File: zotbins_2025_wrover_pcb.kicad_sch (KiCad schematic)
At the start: 18 parts, among them J1 ov2640, J2 hcsr04, J3 hx711, J4 infrared, U1 ESP32-WROVER-E/IE-DEVKIT-C, U2 MCP23017_SP, U3 XC6206P122MR-G, U4 XC6206P282PR-G

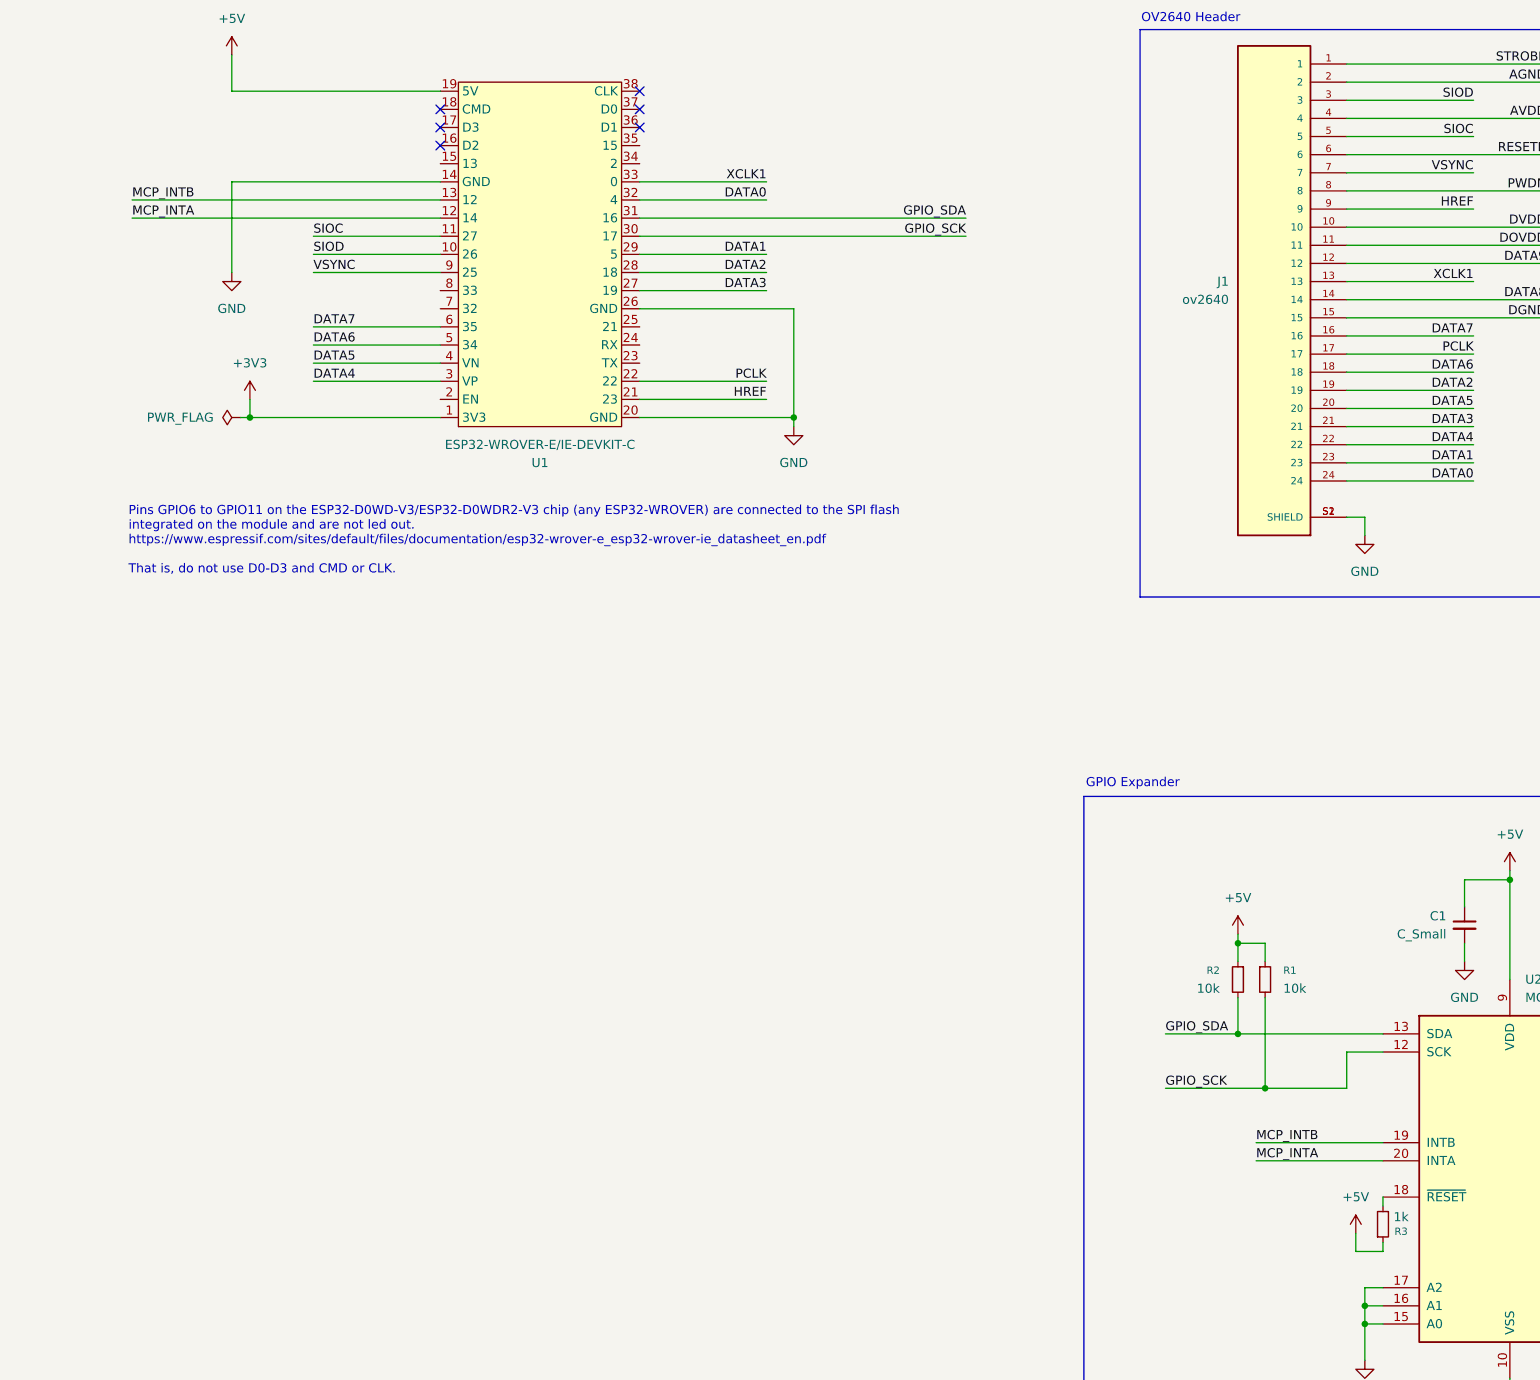
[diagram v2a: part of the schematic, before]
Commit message: pins reconfigured
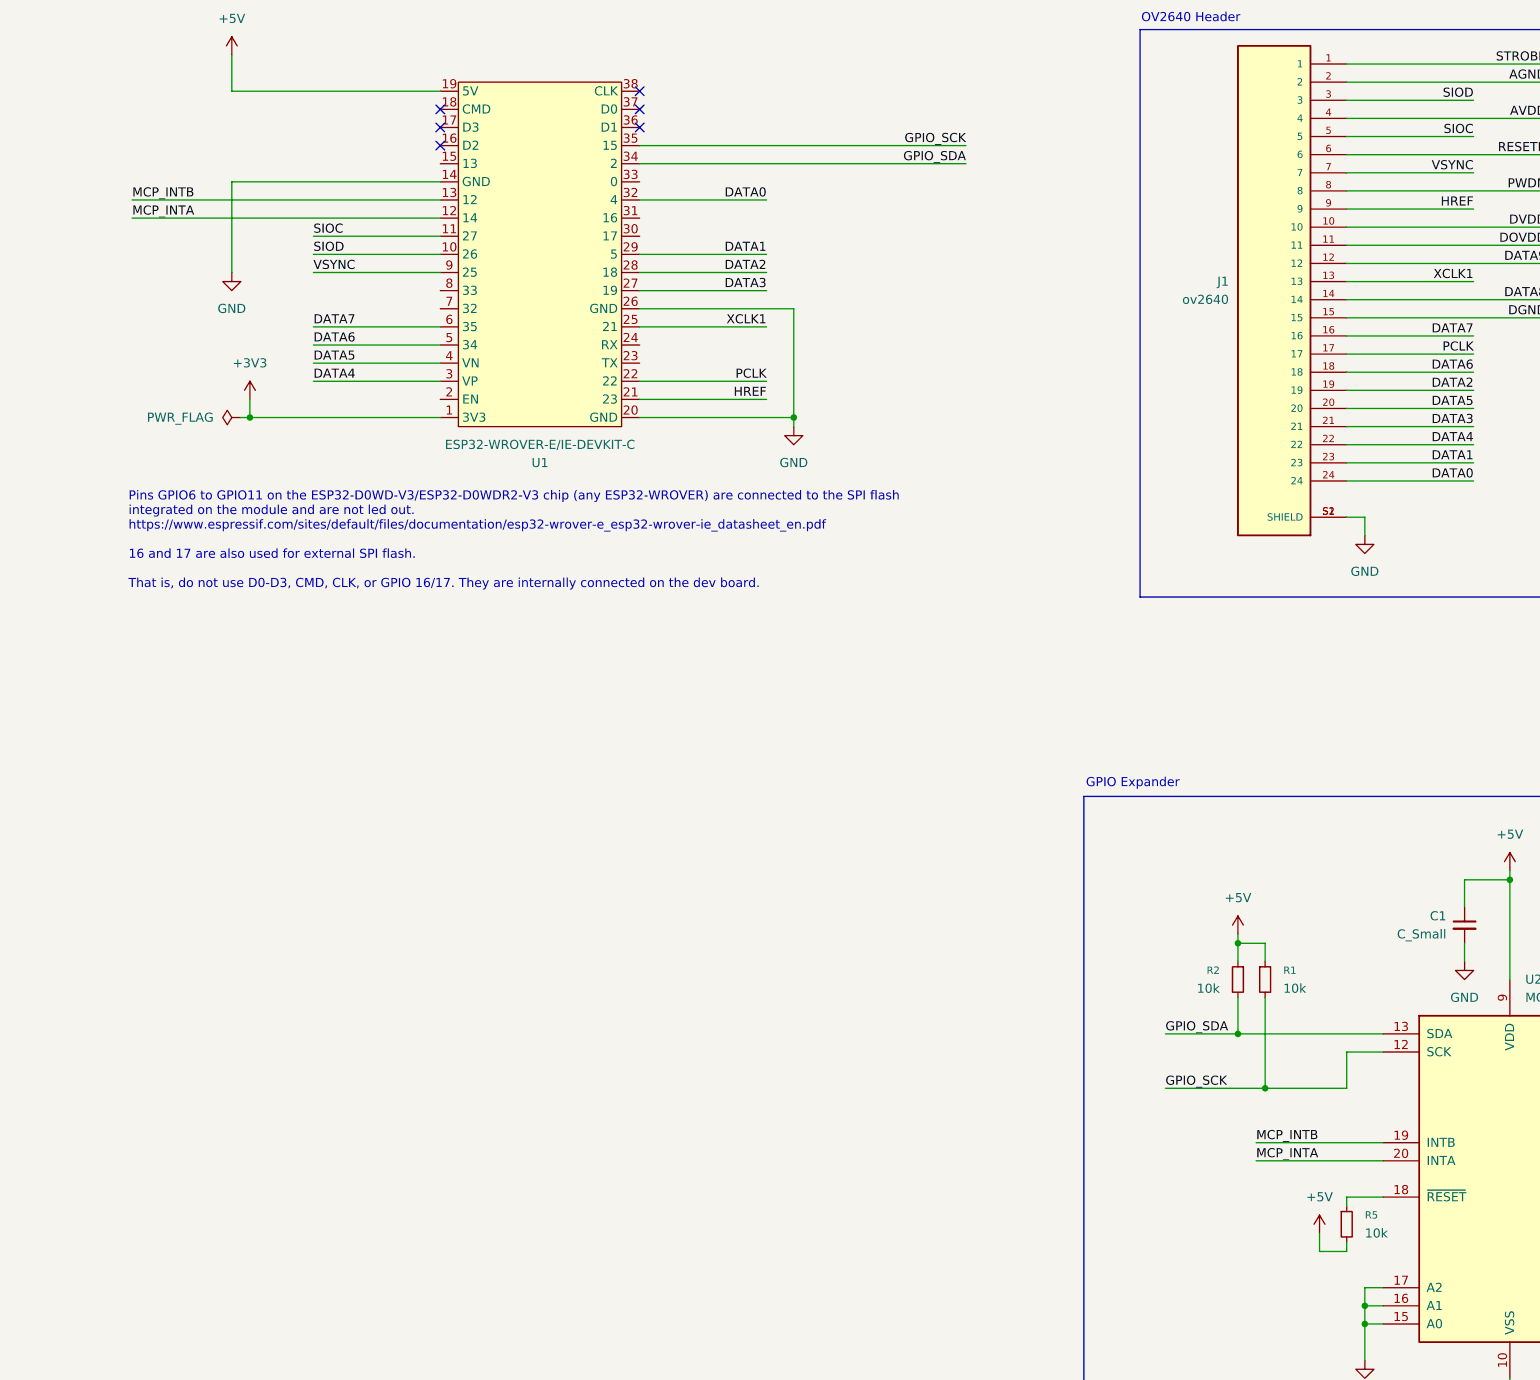
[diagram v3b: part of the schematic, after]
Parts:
- removed R3: 1k, symbol Device:R_Small
- added R5: 10k, symbol Device:R_Small
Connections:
- net +5V: now also R5.2
- net GPIO_SCK: now also U1.35 (15); no longer U1.30 (17)
- net GPIO_SDA: now also U1.34 (2); no longer U1.31 (16)
- net XCLK1: now also U1.25 (21); no longer U1.33 (0)
- net at U2.18 (~{RESET}): now also R5.1
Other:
- note added: "Pins GPIO6 to GPIO11 on the ESP32-D0WD-V3/ESP32-D0WDR2-V3 chip (any ESP32-WROVER) are connected to the SPI flash integrated on the module and are not led out. https://www.espressif.com/sites/default/files/documentation/esp32-wrover-e_esp32-wrover-ie_datasheet_en.pdf 16 and 17 are also used for external SPI flash. That is, do not use D0-D3, CMD, CLK, or GPIO 16/17. They are internally connected on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"
- note removed: "Pins GPIO6 to GPIO11 on the ESP32-D0WD-V3/ESP32-D0WDR2-V3 chip (any ESP32-WROVER) are connected to the SPI flash integrated on the module and are not led out. https://www.espressif.com/sites/default/files/documentation/esp32-wrover-e_esp32-wrover-ie_datasheet_en.pdf That is, do not use D0-D3 and CMD or CLK."
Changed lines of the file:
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@@
 		)
 	)
-	(text "Pins GPIO6 to GPIO11 on the ESP32-D0WD-V3/ESP32-D0WDR2-V3 chip (any ESP32-WROVER) are connected to the SPI flash\nintegrated on the module and are not led out.\nhttps://www.espressif.com/sites/default/files/documentation/esp32-wrover-e_esp32-wrover-ie_datasheet_en.pdf\n\nThat is, do not use D0-D3 and CMD or CLK."
+	(text "Pins GPIO6 to GPIO11 on the ESP32-D0WD-V3/ESP32-D0WDR2-V3 chip (any ESP32-WROVER) are connected to the SPI flash\nintegrated on the module and are not led out.\nhttps://www.espressif.com/sites/default/files/documentation/esp32-wrover-e_esp32-wrover-ie_datasheet_en.pdf\n\n16 and 17 are also used for external SPI flash.\n\nThat is, do not use D0-D3, CMD, CLK, or GPIO 16/17. They are internally connected on the dev board."
 		(exclude_from_sim no)
 		(at 136.652 94.742 0)
@@
 	(wire
 		(pts
-			(xy 208.28 52.07) (xy 254 52.07)
+			(xy 325.12 71.12) (xy 307.34 71.12)
 		)
 		(stroke
@@
 	(wire
 		(pts
-			(xy 325.12 71.12) (xy 307.34 71.12)
+			(xy 323.85 142.24) (xy 330.2 142.24)
 		)
 		(stroke
@@
 	(wire
 		(pts
-			(xy 323.85 142.24) (xy 330.2 142.24)
+			(xy 41.91 33.02) (xy 52.07 33.02)
 		)
 		(stroke
@@
 	(wire
 		(pts
-			(xy 41.91 33.02) (xy 52.07 33.02)
+			(xy 137.16 46.99) (xy 180.34 46.99)
 		)
 		(stroke
@@
 	(wire
 		(pts
-			(xy 137.16 46.99) (xy 180.34 46.99)
+			(xy 307.34 194.31) (xy 303.53 194.31)
 		)
 		(stroke
@@
 	(wire
 		(pts
-			(xy 312.42 194.31) (xy 308.61 194.31)
+			(xy 208.28 39.37) (xy 254 39.37)
 		)
 		(stroke
@@
 	(wire
 		(pts
-			(xy 226.06 44.45) (xy 208.28 44.45)
-		)
-		(stroke
-			(width 0)
-			(type default)
-		)
-	)
-	(wire
-		(pts
 			(xy 363.22 71.12) (xy 381 71.12)
 		)
@@
 	(wire
 		(pts
-			(xy 312.42 187.96) (xy 312.42 186.69)
+			(xy 307.34 187.96) (xy 307.34 186.69)
 		)
 		(stroke
@@
 	(wire
 		(pts
-			(xy 308.61 191.77) (xy 308.61 194.31)
+			(xy 303.53 191.77) (xy 303.53 194.31)
 		)
 		(stroke
@@
 	(wire
 		(pts
+			(xy 307.34 186.69) (xy 312.42 186.69)
+		)
+		(stroke
+			(width 0)
+			(type default)
+		)
+	)
+	(wire
+		(pts
 			(xy 340.36 83.82) (xy 358.14 83.82)
 		)
@@
 	(wire
 		(pts
+			(xy 226.06 64.77) (xy 208.28 64.77)
+		)
+		(stroke
+			(width 0)
+			(type default)
+		)
+	)
+	(wire
+		(pts
 			(xy 373.38 161.29) (xy 363.22 161.29)
 		)
@@
 	(wire
 		(pts
-			(xy 312.42 193.04) (xy 312.42 194.31)
+			(xy 307.34 193.04) (xy 307.34 194.31)
 		)
 		(stroke
@@
 	(wire
 		(pts
-			(xy 208.28 49.53) (xy 254 49.53)
-		)
-		(stroke
-			(width 0)
-			(type default)
-		)
-	)
-	(wire
-		(pts
 			(xy 292.1 151.13) (xy 292.1 153.67)
 		)
@@
 	(wire
 		(pts
+			(xy 208.28 41.91) (xy 254 41.91)
+		)
+		(stroke
+			(width 0)
+			(type default)
+		)
+	)
+	(wire
+		(pts
 			(xy 295.91 158.75) (xy 295.91 171.45)
 		)
@@
 		)
 	)
+	(label "GPIO_SDA"
+		(at 254 41.91 180)
+		(effects
+			(font
+				(size 1.27 1.27)
+			)
+			(justify right bottom)
+		)
+	)
 	(label "MCP_INTA"
 		(at 294.64 181.61 0)
@@
 	)
 	(label "XCLK1"
-		(at 226.06 44.45 180)
+		(at 226.06 64.77 180)
 		(effects
 			(font
@@
 		)
 	)
-	(label "GPIO_SDA"
-		(at 254 49.53 180)
-		(effects
-			(font
-				(size 1.27 1.27)
-			)
-			(justify right bottom)
-		)
-	)
 	(label "VSYNC"
 		(at 162.56 57.15 0)
@@
 		)
 	)
+	(label "GPIO_SCK"
+		(at 254 39.37 180)
+		(effects
+			(font
+				(size 1.27 1.27)
+			)
+			(justify right bottom)
+		)
+	)
 	(label "DATA1"
 		(at 226.06 54.61 180)
@@
 		)
 	)
-	(label "GPIO_SCK"
-		(at 254 52.07 180)
-		(effects
-			(font
-				(size 1.27 1.27)
-			)
-			(justify right bottom)
-		)
-	)
 	(label "AVDD"
 		(at 335.28 35.56 180)
@@
 	)
 	(symbol
+		(lib_id "Device:R_Small")
+		(at 307.34 190.5 0)
+		(unit 1)
+		(exclude_from_sim no)
+		(in_bom yes)
+		(on_board yes)
+		(dnp no)
+		(fields_autoplaced yes)
+		(property "Reference" "R5"
+			(at 309.88 189.2299 0)
+			(effects
+				(font
+					(size 1.016 1.016)
+				)
+				(justify left)
+			)
+		)
+		(property "Value" "10k"
+			(at 309.88 191.7699 0)
+			(effects
+				(font
+					(size 1.27 1.27)
+				)
+				(justify left)
+			)
+		)
+		(property "Footprint" ""
+			(at 307.34 190.5 0)
+			(effects
+				(font
+					(size 1.27 1.27)
+				)
+				(hide yes)
+			)
+		)
+		(property "Datasheet" "~"
+			(at 307.34 190.5 0)
+			(effects
+				(font
+					(size 1.27 1.27)
+				)
+				(hide yes)
+			)
+		)
+		(property "Description" "Resistor, small symbol"
+			(at 307.34 190.5 0)
+			(effects
+				(font
+					(size 1.27 1.27)
+				)
+				(hide yes)
+			)
+		)
+		(pin "1"
+		)
+		(pin "2"
+		)
+		(instances
+			(project "zotbins_2025_wrover_pcb"
+				(path "/aba5dde1-d626-46ae-bab9-bd846b47c317"
+					(reference "R5")
+					(unit 1)
+				)
+			)
+		)
+	)
+	(symbol
 		(lib_id "Connector:Screw_Terminal_01x04")
 		(at 378.46 176.53 0)
@@
 	)
 	(symbol
-		(lib_id "Device:R_Small")
-		(at 312.42 190.5 0)
-		(mirror x)
-		(unit 1)
-		(exclude_from_sim no)
-		(in_bom yes)
-		(on_board yes)
-		(dnp no)
-		(property "Reference" "R3"
-			(at 314.96 191.516 0)
-			(effects
-				(font
-					(size 1.016 1.016)
-				)
-			)
-		)
-		(property "Value" "1k"
-			(at 314.96 189.484 0)
-			(effects
-				(font
-					(size 1.27 1.27)
-				)
-			)
-		)
-		(property "Footprint" ""
-			(at 312.42 190.5 0)
-			(effects
-				(font
-					(size 1.27 1.27)
-				)
-				(hide yes)
-			)
-		)
-		(property "Datasheet" "~"
-			(at 312.42 190.5 0)
-			(effects
-				(font
-					(size 1.27 1.27)
-				)
-				(hide yes)
-			)
-		)
-		(property "Description" "Resistor, small symbol"
-			(at 312.42 190.5 0)
-			(effects
-				(font
-					(size 1.27 1.27)
-				)
-				(hide yes)
-			)
-		)
-		(pin "1"
-		)
-		(pin "2"
-		)
-		(instances
-			(project "zotbins_2025_wrover_pcb"
-				(path "/aba5dde1-d626-46ae-bab9-bd846b47c317"
-					(reference "R3")
-					(unit 1)
-				)
-			)
-		)
-	)
-	(symbol
 		(lib_id "Regulator_Linear:XC6206P122MR-G")
 		(at 59.69 33.02 0)
@@
 	(symbol
 		(lib_id "power:+5V")
-		(at 308.61 191.77 0)
+		(at 303.53 191.77 0)
 		(unit 1)
 		(exclude_from_sim no)
@@
 		(fields_autoplaced yes)
 		(property "Reference" "#PWR09"
-			(at 308.61 195.58 0)
+			(at 303.53 195.58 0)
 			(effects
 				(font
@@
 		)
 		(property "Value" "+5V"
-			(at 308.61 186.69 0)
+			(at 303.53 186.69 0)
 			(effects
 				(font
@@
 		)
 		(property "Footprint" ""
-			(at 308.61 191.77 0)
+			(at 303.53 191.77 0)
 			(effects
 				(font
@@
 		)
 		(property "Datasheet" ""
-			(at 308.61 191.77 0)
+			(at 303.53 191.77 0)
 			(effects
 				(font
@@
 		)
 		(property "Description" "Power symbol creates a global label with name \"+5V\""
-			(at 308.61 191.77 0)
+			(at 303.53 191.77 0)
 			(effects
 				(font

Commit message: added footprints
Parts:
- removed J1: ov2640, FFC2B28-24-G:GCT_FFC2B28-24-G, symbol FFC2B28-24-G:FFC2B28-24-G
- removed J2: hcsr04, symbol Connector:Screw_Terminal_01x04
- removed J3: hx711, symbol Connector:Screw_Terminal_01x04
- removed J4: infrared, symbol Connector:Screw_Terminal_01x03
- added C7: 0.33u, Capacitor_THT:C_Disc_D4.3mm_W1.9mm_P5.00mm, symbol Device:C_Small
- added C8: 0.1u, Capacitor_THT:C_Disc_D4.3mm_W1.9mm_P5.00mm, symbol Device:C_Small
- added J1: FFC2B28-24-G, Connector_FFC-FPC:GCT_FFC2B28-24-G, symbol Connector:FFC2B28-24-G
- added J5: DCJ200-10-A-XX-K_REVA, Connector_BarrelJack:GCT_DCJ200-10-A-XX-K_REVA, symbol Converter_DCDC:DCJ200-10-A-XX-K_REVA
- added J6: Conn_01x30_Pin, Connector_PinSocket_2.54mm:PinSocket_2x15_P2.54mm_Vertical, symbol Connector:Conn_01x30_Pin
- added TP1, TP2, TP3, TP4, TP5, TP6: TestPoint, TestPoint:TestPoint_Keystone_5005-5009_Compact, symbol Connector:TestPoint
- added U5: LM7805_TO220, Package_TO_SOT_THT:TO-220-3_Vertical, symbol Regulator_Linear:LM7805_TO220
- C1: value C_Small -> 1u; footprint (none) -> Capacitor_THT:C_Disc_D4.3mm_W1.9mm_P5.00mm
- C2, C3, C4, C5, C6: footprint (none) -> Capacitor_THT:C_Disc_D4.3mm_W1.9mm_P5.00mm
- R1, R2, R4, R5: footprint (none) -> Resistor_THT:R_Axial_DIN0207_L6.3mm_D2.5mm_P10.16mm_Horizontal
- U1: footprint (none) -> MCU_Development_Board:MODULE_ESP32-DEVKITC-32D
- U3, U4: footprint Package_TO_SOT_THT:TO-220-3_Vertical -> Package_TO_SOT_SMD:SOT-23
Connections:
- net +3.3V is gone; now on net +3V3: R4.1
- net +3V3: now also J1.11, TP6.1
- net +5V: now also C8.1, J6.28 (Pin_28), J6.29 (Pin_29), J6.30 (Pin_30), TP3.1, U5.3 (VO)
- net CSI_1V2: now also J1.10, TP2.1
- net CSI_2V8: now also J1.4, TP1.1
- net DATA0: now also J1.24
- net DATA1: now also J1.23
- net DATA2: now also J1.19
- net DATA3: now also J1.21
- net DATA4: now also J1.22
- net DATA5: now also J1.20
- net DATA6: now also J1.18
- net DATA7: now also J1.16
- net DATA8: now also J1.14
- net DATA9: now also J1.12
- net DT: now also J6.21 (Pin_21)
- net ECHO: now also J6.23 (Pin_23)
- net GND: now also C7.2, C8.2, J1.1, J1.15, J1.2, J1.8, J1.S1 (SHIELD), J1.S2 (SHIELD__1), J5.2, J5.3, J6.25 (Pin_25), J6.26 (Pin_26), J6.27 (Pin_27), TP4.1, U5.2 (GND)
- net GPIO_SCK: now also R2.2, U2.13 (SDA); no longer R1.2, U2.12 (SCK)
- net GPIO_SDA: now also R1.2, U2.12 (SCK); no longer R2.2, U2.13 (SDA)
- net HREF: now also J1.9
- net MCP_INTA: now also U1.13 (12); no longer U1.12 (14)
- net MCP_INTB: now also U1.12 (14); no longer U1.13 (12)
- net PCLK: now also J1.17
- net RESETB: now also J1.6
- net SCK: now also J6.22 (Pin_22)
- net SIOC: now also J1.5
- net SIOD: now also J1.3
- net TRIG: now also J6.24 (Pin_24)
- net VSYNC: now also J1.7
- net XCLK1: now also J1.13
- net GPA0: now reaches U2.21 (GPA0)
- net GPA0: now also J6.15 (Pin_15)
- net GPIO13: now reaches U1.15 (13)
- net GPIO13: now also J6.14 (Pin_14)
- net EN: now reaches U1.2 (EN)
- net EN: now also J6.6 (Pin_6)
- net TX: now reaches U1.23 (TX)
- net TX: now also J6.2 (Pin_2)
- net RX: now reaches U1.24 (RX)
- net RX: now also J6.4 (Pin_4)
- net GPIO0: now reaches U1.33 (0)
- net GPIO0: now also J6.12 (Pin_12)
- net GPIO32: now reaches U1.7 (32)
- net GPIO32: now also J6.8 (Pin_8)
- net GPIO33: now reaches U1.8 (33)
- net GPIO33: now also J6.10 (Pin_10)
- net GPA1: now reaches U2.22 (GPA1)
- net GPA1: now also J6.13 (Pin_13)
- net GPA2: now reaches U2.23 (GPA2)
- net GPA2: now also J6.11 (Pin_11)
- net GPA3: now reaches U2.24 (GPA3)
- net GPA3: now also J6.9 (Pin_9)
- net GPA4: now reaches U2.25 (GPA4)
- net GPA4: now also J6.7 (Pin_7)
- net GPA5: now reaches U2.26 (GPA5)
- net GPA5: now also J6.5 (Pin_5)
- net GPA6: now reaches U2.27 (GPA6)
- net GPA6: now also J6.3 (Pin_3)
- net GPA7: now reaches U2.28 (GPA7)
- net GPA7: now also J6.1 (Pin_1)
- net GPB4: now reaches U2.5 (GPB4)
- net GPB4: now also J6.17 (Pin_17)
- net GPB5: now reaches U2.6 (GPB5)
- net GPB5: now also J6.19 (Pin_19)
- net GPB6: now reaches U2.7 (GPB6)
- net GPB6: now also J6.20 (Pin_20)
- net IR: now reaches U2.8 (GPB7)
- net IR: now also J6.16 (Pin_16)
- new net: C7.1, J5.1, TP5.1, U5.1 (VI)
- no-connect marks 8 -> 11
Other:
- moved on the sheet: C1, C2, C3, C4, C5, C6, R1, R2, R4, R5, U1, U2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
